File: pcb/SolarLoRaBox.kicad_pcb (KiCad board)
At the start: 4 copper layers, 71.3 x 92.8 mm, 56 parts, among them J1 Conn_01x02_Socket, J2 Conn_01x02_Socket, J3 Conn_01x04_Socket, J4 Conn_ARM_SWD_TagConnect_TC2030, J5 Conn_01x04_Socket, J6 Conn_01x04_Socket, J7 Conn_01x04_Socket, J8 Conn_01x04_Socket, SW1 SSSS811101, SW2 SW_Push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

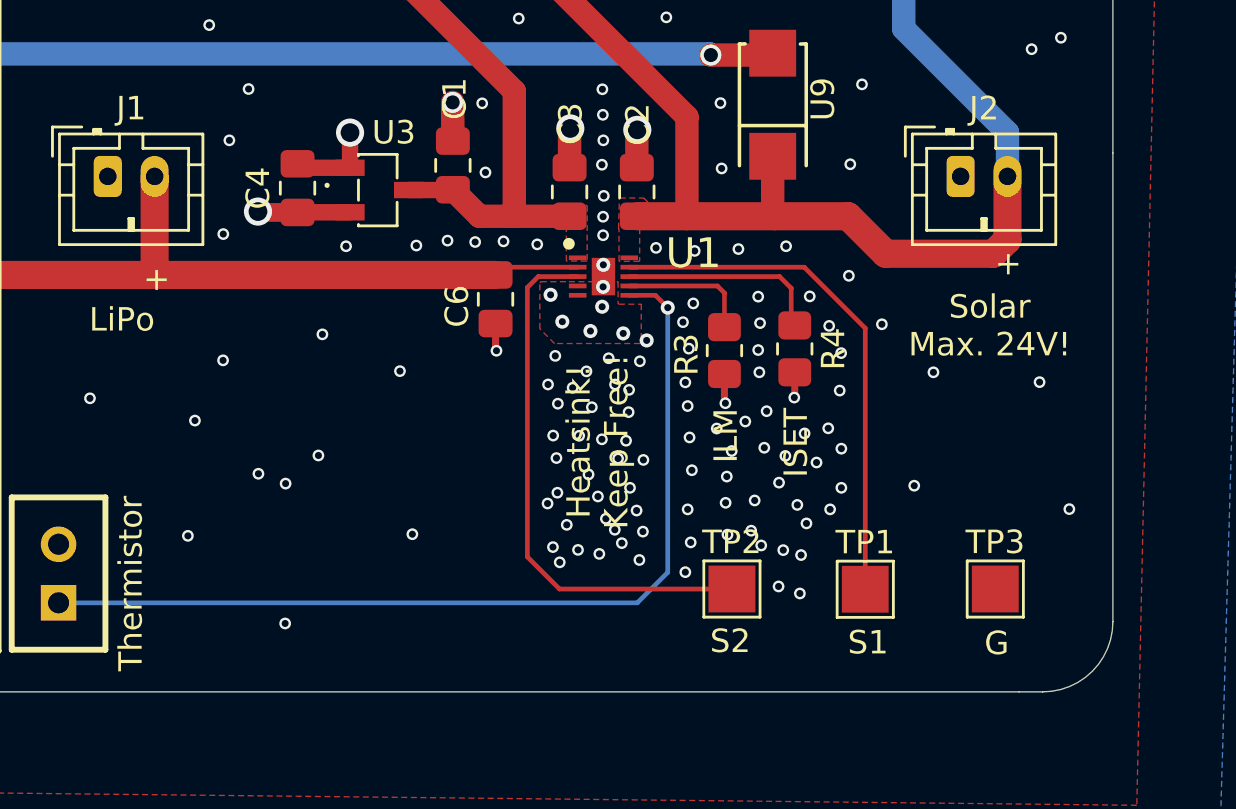
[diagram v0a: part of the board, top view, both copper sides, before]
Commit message: pcb: rework heatsink area below the solar charging controller
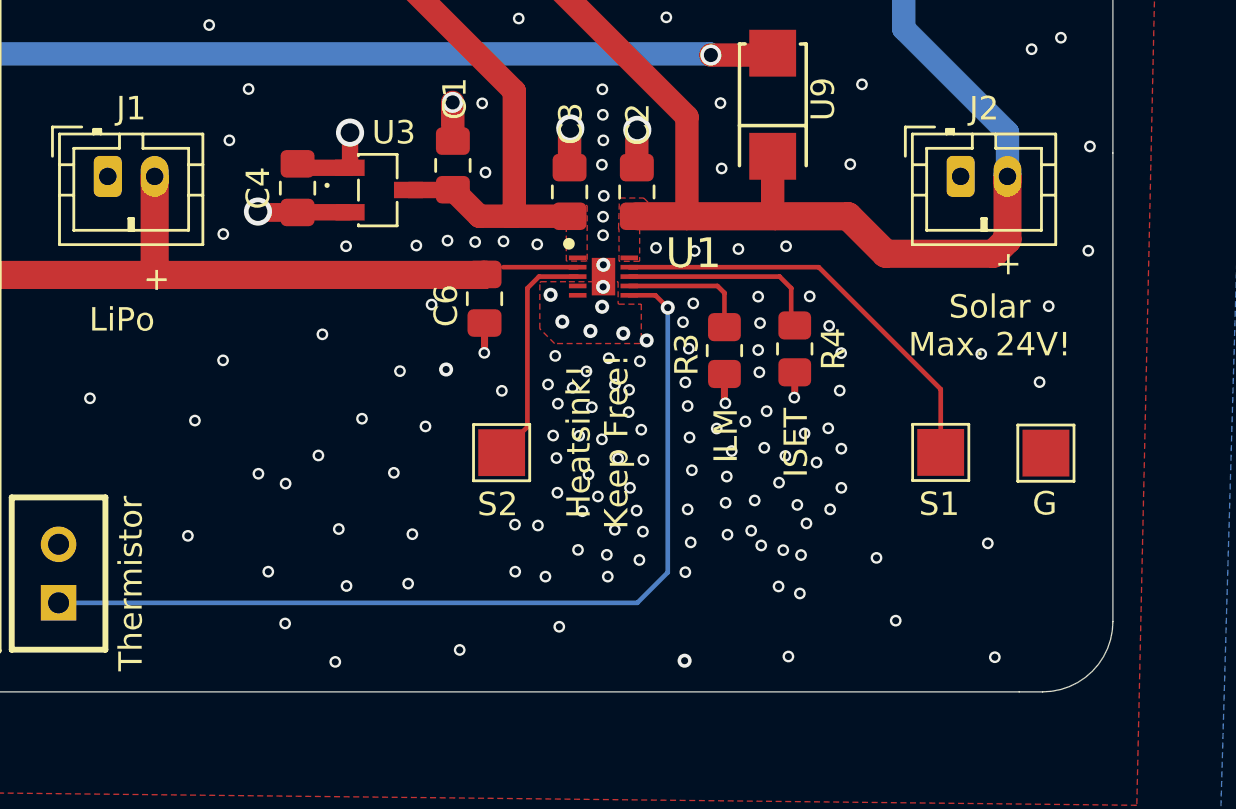
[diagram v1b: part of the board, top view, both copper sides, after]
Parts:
- moved TP2 11.4 mm to (228.3, 111.9)
- moved TP1 6.67 mm to (247.1, 111.9)
- moved TP3 6.19 mm to (251.5, 111.9)
- moved C6 0.47 mm to (227.6, 105.3)
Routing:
- net Net-(U1-STAT2): track 23.1 -> 9.83 mm
- net Net-(U1-STAT1): track 22.3 -> 18.1 mm
- net GND: track 56.2 -> 56.3 mm, vias 424 -> 442

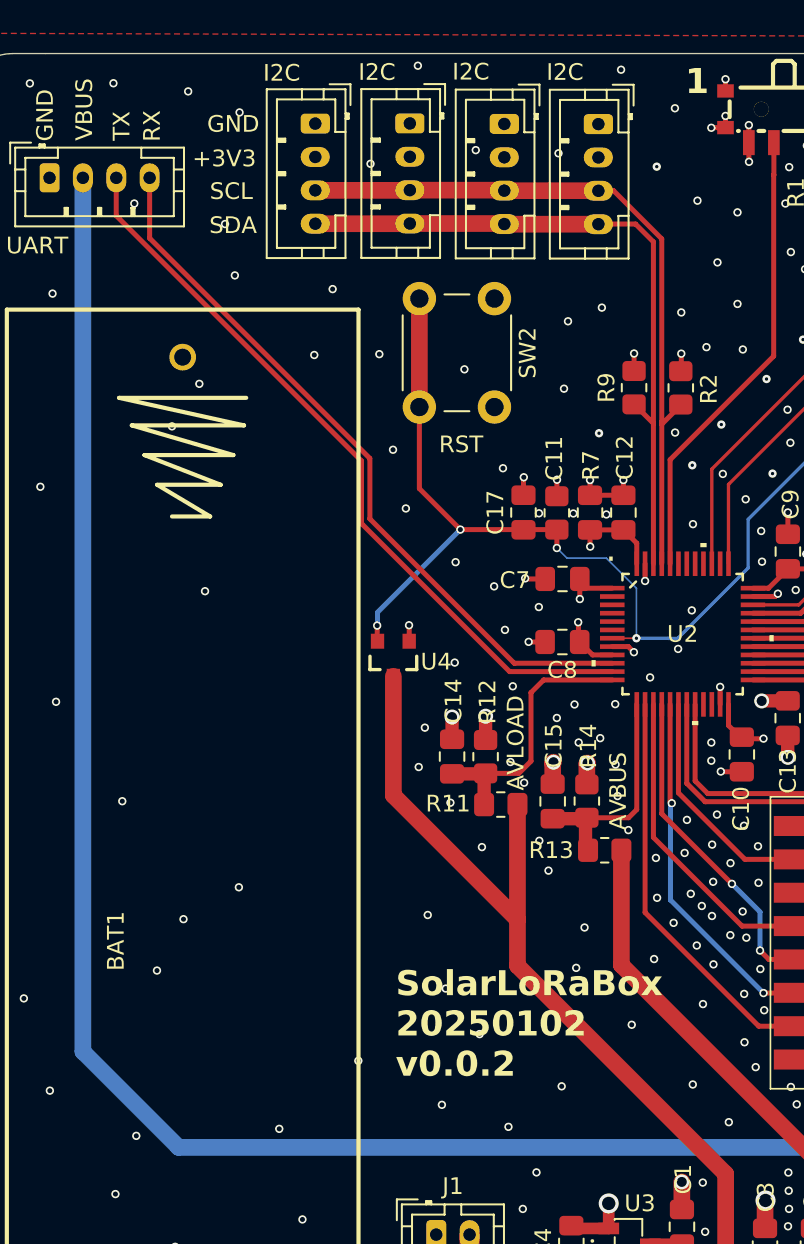
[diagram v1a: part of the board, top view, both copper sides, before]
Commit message: pcb, sch: fix invalid uart rx/tx silk print, add C infront of reset ic
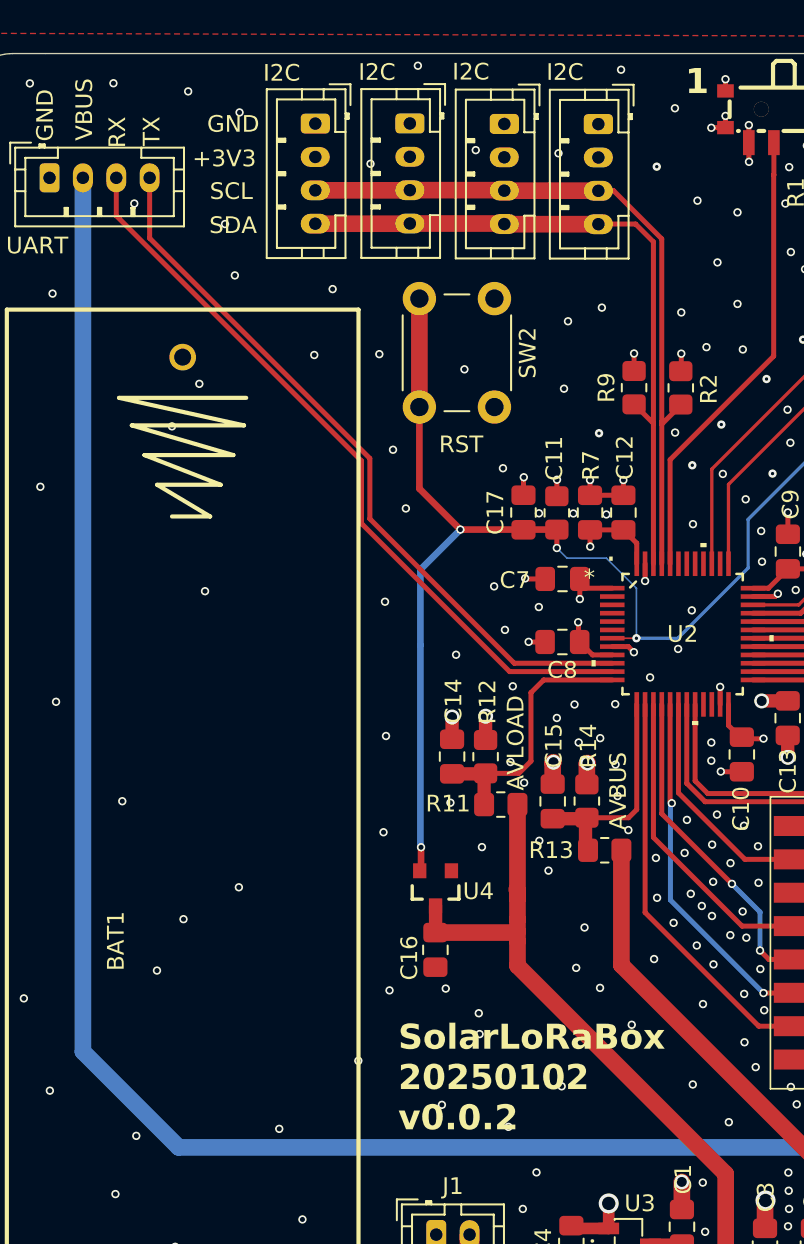
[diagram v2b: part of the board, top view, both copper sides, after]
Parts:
- added C16: 1uF, Capacitor_SMD:C_0805_2012Metric_Pad1.18x1.45mm_HandSolder, F.Cu at (211.4, 83.0)
- moved U4 14.0 mm to (211.5, 79.3)
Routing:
- net /RESET: track 88.7 -> 101.6 mm
- net /VLOAD: track 57.6 -> 47.1 mm
- net GND: track 56.3 -> 55.3 mm, vias 442 -> 443

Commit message: Updates pictures and reorganize structure a bit
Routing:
- net GND: vias 443 -> 445
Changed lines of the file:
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@@
 		(descr "SOT23-3")
 		(property "Reference" "U4"
-			(at -2.57 -0.23 360)
+			(at -2.57 -0.23 0)
 			(layer "F.SilkS")
 			(effects
@@
 		)
 		(property "Value" "APX803L05-32SA-7"
-			(at 1.9558 0 360)
+			(at 1.9558 0 0)
 			(layer "F.Fab")
 			(hide yes)
@@
 		)
 		(property "Footprint" "footprints:SOT23-3"
-			(at 0 0 360)
+			(at 0 0 0)
 			(layer "F.Fab")
 			(hide yes)
@@
 		)
 		(property "Datasheet" "https://wmsc.lcsc.com/wmsc/upload/file/pdf/v2/lcsc/2304140030_Diodes-Incorporated-APX803L05-32SA-7_C2067928.pdf"
-			(at 0 0 360)
+			(at 0 0 0)
 			(layer "F.Fab")
 			(hide yes)
@@
 		)
 		(property "Description" "35ms Active Low 1 SOT-23 Supervisor and Reset ICs ROHS"
-			(at 0 0 360)
+			(at 0 0 0)
 			(layer "F.Fab")
 			(hide yes)
@@
 	)
 	(via
+		(at 214.46 80.62)
+		(size 0.4)
+		(drill 0.2)
+		(layers "F.Cu" "B.Cu")
+		(free yes)
+		(net 2)
+	)
+	(via
 		(at 195.66 51.65)
 		(size 0.5)
@@
 		(layers "F.Cu" "B.Cu")
 		(free yes)
+		(net 2)
+	)
+	(via
+		(at 208.56 80.54)
+		(size 0.4)
+		(drill 0.2)
+		(layers "F.Cu" "B.Cu")
+		(free yes)

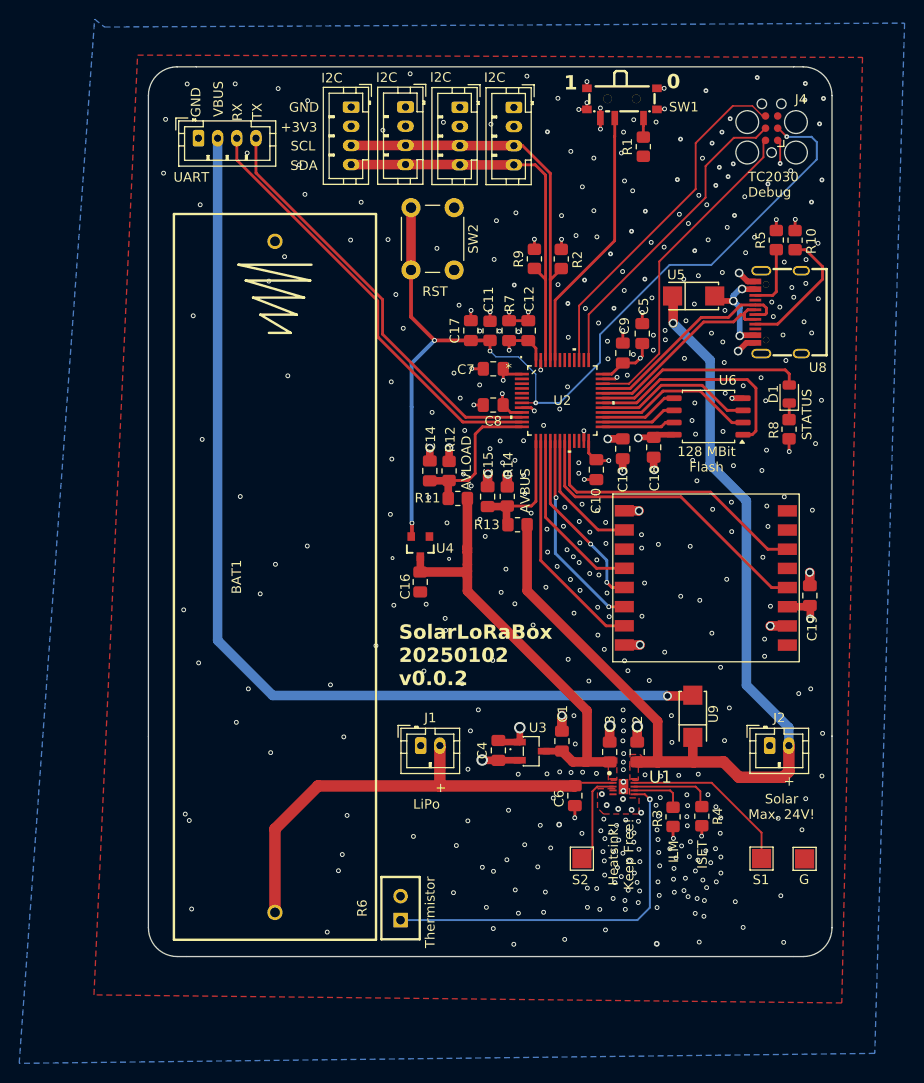
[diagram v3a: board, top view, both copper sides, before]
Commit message: pcb, sch, doc: lots of cosmetic fixes
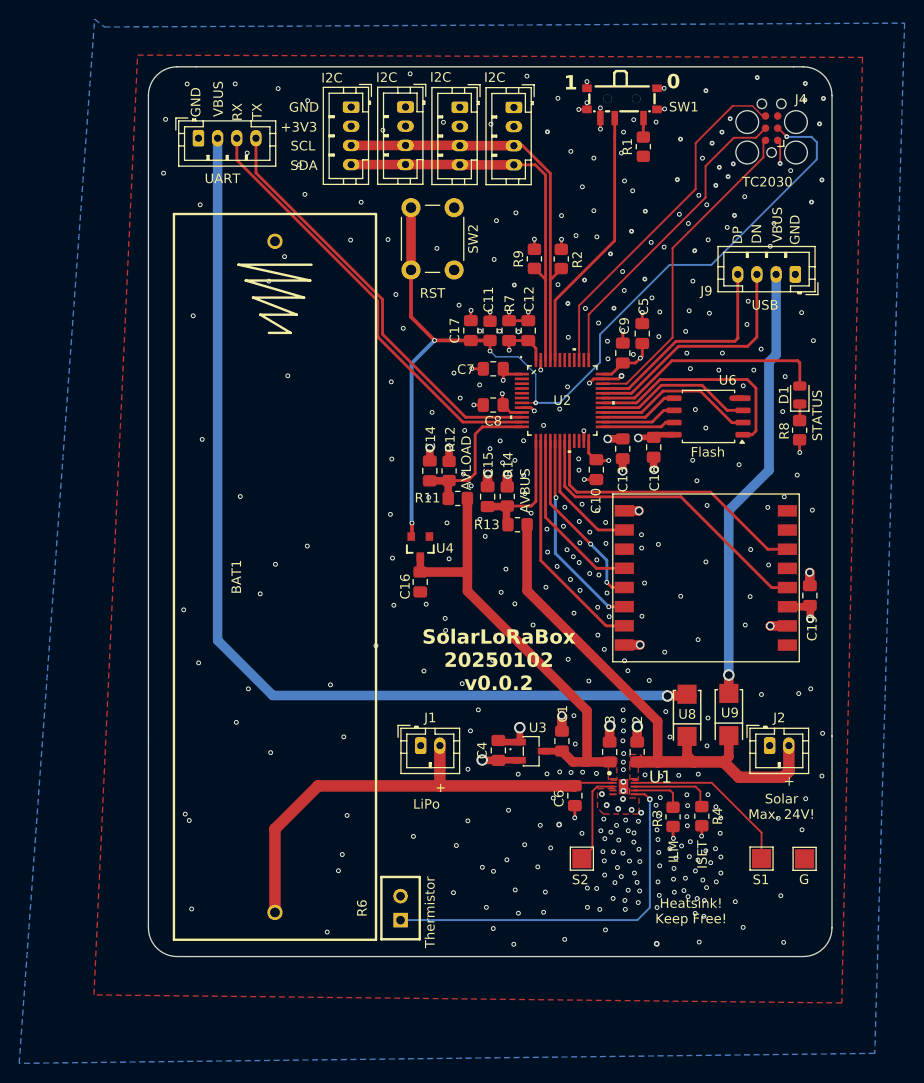
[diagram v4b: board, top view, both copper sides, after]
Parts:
- removed R10, R5: 5.1k, Resistor_SMD:R_0805_2012Metric_Pad1.20x1.40mm_HandSolder
- removed U5: SS26_C5350986, footprints:SMA_L4.3-W2.6-LS5.1-RD
- added J9: Conn_01x04_Socket, Connector_JST:JST_PH_B4B-PH-K_1x04_P2.00mm_Vertical, F.Cu at (250.6, 51.0)
- U8: value GT-USB-7010ASV -> SS26_C5350986; footprint footprints:USB-C-SMD_G-SWITCH_GT-USB-7010ASV -> footprints:SMA_L4.3-W2.6-LS5.1-RD
- moved U8 42.3 mm to (243.6, 96.9)
- moved D1 1.10 mm to (251.0, 63.5)
- moved R8 1.10 mm to (251.0, 67.2)
- moved U9 0.61 mm to (239.3, 96.9)
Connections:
- U8 pad 1: unconnected-(U8-SHELL-Pad1) -> /VBUS
- U8 pad 2: unconnected-(U8-SHELL-Pad2) -> Net-(J9-Pin_2)
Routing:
- net /VBUS: track 103.8 -> 55.7 mm, vias 1 -> 0
- net Net-(J9-Pin_2): track 0.00 -> 45.8 mm, vias 0 -> 1
- net Net-(U8-CC1): track 13.9 -> 0.00 mm
- net Net-(U5-A): track 10.5 -> 0.00 mm, vias 3 -> 0
- net Net-(U8-CC2): track 6.74 -> 0.00 mm
- net GND: track 55.3 -> 50.9 mm, vias 445 -> 416
- net /USB_DN: track 21.2 -> 25.0 mm
- net /LED_STATUS: track 22.0 -> 24.7 mm
- net /VLOAD: track 47.1 -> 46.5 mm
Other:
- board text added: "DN"
- board text added: "DP"
- board text added: "Flash"
- board text added: "TC2030"
- board text added: "USB"
- board text removed: "128 MBit Flash"
- board text removed: "TC2030 Debug"

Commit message: pcb, sch: more eyecandy
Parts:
- moved U8 1.57 mm to (242.1, 96.8)
- moved U9 0.51 mm to (238.8, 96.9)
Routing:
- net /USB_DP: track 22.9 -> 19.3 mm
- net /USB_DN: track 25.0 -> 21.8 mm
- net /VBUS: track 55.7 -> 57.7 mm
- net /RESET: track 101.3 -> 102.5 mm
- net Net-(J3-Pin_2): track 104.3 -> 103.4 mm
- net Net-(J9-Pin_2): track 45.8 -> 46.4 mm
- net GND: vias 416 -> 423

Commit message: pcb, sch: switch MISO/MOSI on Windbond flash as they are inverted!
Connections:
- U6 pad 2: /FLASH_MOSI -> /FLASH_MISO
- U6 pad 5: /FLASH_MISO -> /FLASH_MOSI
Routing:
- net /FLASH_MOSI: track 16.4 -> 8.05 mm
- net /FLASH_MISO: track 8.26 -> 15.9 mm, vias 0 -> 2
- net /USB_DP: track 19.3 -> 18.8 mm
- net GND: vias 423 -> 426
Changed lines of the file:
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@@
 			(layers "F.Cu" "F.Paste" "F.Mask")
 			(roundrect_rratio 0.25)
-			(net 46 "/FLASH_MOSI")
+			(net 36 "/FLASH_MISO")
 			(pinfunction "DO(IO1)")
 			(pintype "bidirectional")
@@
 			(layers "F.Cu" "F.Paste" "F.Mask")
 			(roundrect_rratio 0.25)
-			(net 36 "/FLASH_MISO")
+			(net 46 "/FLASH_MOSI")
 			(pinfunction "DI(IO0)")
 			(pintype "bidirectional")
@@
 			(layer "F.Fab")
 		)
-		(fp_text user "${REFERENCE}"
-			(at 0 0 0)
+		(fp_text user "*"
+			(at -5.588 -3.381 0)
 			(unlocked yes)
 			(layer "F.Fab")
@@
 			)
 		)
-		(fp_text user "*"
-			(at -5.588 -3.381 0)
+		(fp_text user "${REFERENCE}"
+			(at 0 0 0)
 			(unlocked yes)
 			(layer "F.Fab")
@@
 			(pintype "power_in")
 		)
-		(model "${KICAD8_3DMODEL_DIR}/Package_DFN_QFN.3dshapes/UQFN-48-1EP_6x6mm_P0.4mm_EP4.45x4.45mm.step"
-			(offset
-				(xyz 0 0 0)
-			)
-			(scale
-				(xyz 1 1 1)
-			)
-			(rotate
-				(xyz 0 0 0)
-			)
-		)
-		(model "${KICAD8_3DMODEL_DIR}/Package_QFP.3dshapes/LQFP-48-1EP_7x7mm_P0.5mm_EP3.6x3.6mm.wrl"
-			(offset
-				(xyz 0 0 0)
-			)
-			(scale
-				(xyz 1 1 1)
-			)
-			(rotate
-				(xyz 0 0 0)
-			)
-		)
 	)
 	(footprint "Resistor_SMD:R_0805_2012Metric_Pad1.20x1.40mm_HandSolder"
@@
 	)
 	(via
+		(at 237.93 69.33)
+		(size 0.5)
+		(drill 0.3)
+		(layers "F.Cu" "B.Cu")
+		(free yes)
+		(net 2)
+	)
+	(via
 		(at 236.55 103.28)
 		(size 0.5)
@@
 	)
 	(via
+		(at 239.87 66.81)
+		(size 0.5)
+		(drill 0.3)
+		(layers "F.Cu" "B.Cu")
+		(free yes)
+		(net 2)
+	)
+	(via
 		(at 188.5 43.69)
 		(size 0.5)
@@
 	)
 	(via
-		(at 240.15 65.05)
-		(size 0.5)
-		(drill 0.3)
-		(layers "F.Cu" "B.Cu")
-		(free yes)
-		(net 2)
-	)
-	(via
 		(at 211.84 92.32)
 		(size 0.5)
@@
 	)
 	(via
+		(at 240.17 63.69)
+		(size 0.5)
+		(drill 0.3)
+		(layers "F.Cu" "B.Cu")
+		(free yes)
+		(net 2)
+	)
+	(via
 		(at 219.4 45.35)
 		(size 0.5)
@@
 	)
 	(via
+		(at 229.87 68.77)
+		(size 0.5)
+		(drill 0.3)
+		(layers "F.Cu" "B.Cu")
+		(free yes)
+		(net 2)
+	)
+	(via
 		(at 241.37 75.05)
 		(size 0.5)
@@
 		(net 10)
 	)
-	(segment
-		(start 236.45 94.87)
-		(end 236.5 94.92)
-		(width 1)
-		(layer "F.Cu")
-		(net 10)
-	)
-	(segment
-		(start 238.57 94.87)
-		(end 238.77 94.67)
-		(width 1)
-		(layer "F.Cu")
-		(net 10)
-	)
 	(via
 		(at 236.45 94.87)
@@
 	)
 	(segment
-		(start 242.07 99.04)
-		(end 241.98 99.13)
-		(width 1)
-		(layer "F.Cu")
-		(net 11)
-	)
-	(segment
 		(start 236.22 97.56)
 		(end 222.6 83.94)
@@
 	)
 	(segment
-		(start 244.57 51.490833)
-		(end 244.57 50.95)
-		(width 0.3)
-		(layer "F.Cu")
-		(net 23)
-	)
-	(segment
 		(start 233.210833 62.85)
 		(end 244.57 51.490833)
@@
 	)
 	(segment
-		(start 234.936402 65.849999)
-		(end 236.925001 63.8614)
+		(start 235.140001 65.849999)
+		(end 230.4864 65.849999)
 		(width 0.3)
 		(layer "F.Cu")
@@
 	)
 	(segment
-		(start 236.925001 63.8614)
-		(end 237.920001 63.8614)
+		(start 236.41 64.58)
+		(end 235.140001 65.849999)
+		(width 0.3)
+		(layer "F.Cu")
+		(net 36)
+	)
+	(segment
+		(start 245.118601 66.4)
+		(end 245.120001 66.4014)
 		(width 0.3)
 		(layer "F.Cu")
@@
 	)
 	(segment
-		(start 230.4864 65.849999)
-		(end 234.936402 65.849999)
+		(start 243.69 66.4)
+		(end 245.118601 66.4)
 		(width 0.3)
 		(layer "F.Cu")
 		(net 36)
 	)
+	(via
+		(at 236.41 64.58)
+		(size 0.5)
+		(drill 0.3)
+		(layers "F.Cu" "B.Cu")
+		(net 36)
+	)
+	(via
+		(at 243.69 66.4)
+		(size 0.5)
+		(drill 0.3)
+		(layers "F.Cu" "B.Cu")
+		(net 36)
+	)
+	(segment
+		(start 241.87 64.58)
+		(end 243.69 66.4)
+		(width 0.3)
+		(layer "B.Cu")
+		(net 36)
+	)
+	(segment
+		(start 236.41 64.58)
+		(end 241.87 64.58)
+		(width 0.3)
+		(layer "B.Cu")
+		(net 36)
+	)
 	(segment
 		(start 236.586401 66.85)
@@
 	)
 	(segment
-		(start 243.96 66.41)
-		(end 244.5728 66.41)
+		(start 235.97 63.86)
+		(end 235.9714 63.8614)
 		(width 0.3)
 		(layer "F.Cu")
@@
 	)
 	(segment
-		(start 234.536401 65.35)
-		(end 236.770001 63.1164)
-		(width 0.3)
-		(layer "F.Cu")
-		(net 46)
-	)
-	(segment
-		(start 240.6664 63.1164)
-		(end 243.96 66.41)
+		(start 235.9714 63.8614)
+		(end 237.920001 63.8614)
 		(width 0.3)
 		(layer "F.Cu")
@@
 	)
 	(segment
-		(start 236.770001 63.1164)
-		(end 240.6664 63.1164)
+		(start 230.4864 65.35)
+		(end 234.48 65.35)
 		(width 0.3)
 		(layer "F.Cu")
@@
 	)
 	(segment
-		(start 230.4864 65.35)
-		(end 234.536401 65.35)
+		(start 234.48 65.35)
+		(end 235.97 63.86)
 		(width 0.3)
 		(layer "F.Cu")

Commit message: EVALUATION: ADC verified
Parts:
- added H1: MountingHole, MountingHole:MountingHole_4.3mm_M4_DIN965, F.Cu at (219.6, 111.8)
- added J10: Conn_01x05_Socket, Connector_JST:JST_PH_B5B-PH-K_1x05_P2.00mm_Vertical, F.Cu at (241.9, 33.2)
- moved J4 6.24 mm to (248.2, 41.9)
- moved J9 5.66 mm to (249.1, 56.4), turned to 90 degrees
- moved J3 3.31 mm to (187.8, 33.5)
- moved SW2 2.86 mm to (212.8, 45.9), turned to 0 degrees
- moved C16 1.71 mm to (213.2, 83.1)
- moved R9 1.26 mm to (223.3, 48.1)
- moved R2 1.24 mm to (226.2, 48.1)
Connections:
- U2 pad 40: unconnected-(U2A-PB4-Pad40) -> /GPIO1
- U2 pad 41: unconnected-(U2A-PB5-Pad41) -> /GPIO2
- U2 pad 42: unconnected-(U2A-PB6-Pad42) -> /GPIO3
- U2 pad 43: unconnected-(U2A-PB7-Pad43) -> /GPIO4
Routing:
- net /GPIO1: track 0.00 -> 37.0 mm
- net /GPIO2: track 0.00 -> 36.4 mm
- net /GPIO3: track 0.00 -> 34.7 mm
- net /GPIO4: track 0.00 -> 34.1 mm
- net /DEBUG_SWDIO: track 33.9 -> 27.2 mm
- net /USB_DP: track 18.8 -> 23.7 mm
- net /RESET: track 102.5 -> 97.7 mm
- net /DEBUG_SWO: track 37.0 -> 32.6 mm
- net Net-(J3-Pin_2): track 103.0 -> 106.5 mm
- net /U_TX: track 44.0 -> 47.5 mm
- net /U_RX: track 45.5 -> 49.0 mm
- net /DEBUG_SWCLK: track 33.2 -> 29.8 mm
- net /USB_DN: track 21.8 -> 23.1 mm
- net /I2C1_SDA: track 41.7 -> 42.9 mm
- net Net-(J9-Pin_2): track 46.4 -> 47.4 mm
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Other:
- board text added: "A"
- board text added: "B"
- board text added: "C"
- board text added: "D"
- board text added: "GPIO"
- board text added: "SolarLoRaBox 20250121 v0.0.2"
- board text removed: "SolarLoRaBox 20250102 v0.0.2"
